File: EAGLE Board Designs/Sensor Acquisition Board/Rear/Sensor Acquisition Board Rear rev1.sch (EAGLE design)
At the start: 26 parts, among them J10 JUMPER_0603_, J4 CONNECTOR-SENSOR_NF_S_RA_BLACK, J5 CONNECTOR-SENSOR_NF_S_RA_BLACK, J6 CONNECTOR-SENSOR_NF_S_RA_BLACK, J7 CONNECTOR-SENSOR_NF_S_RA_BLACK, J9 CONNECTOR-CAN_NF_S_RA_BLACK, U1 VOLTAGE_REGULATOR_SOT-223_5V, U2 MCP2562FD

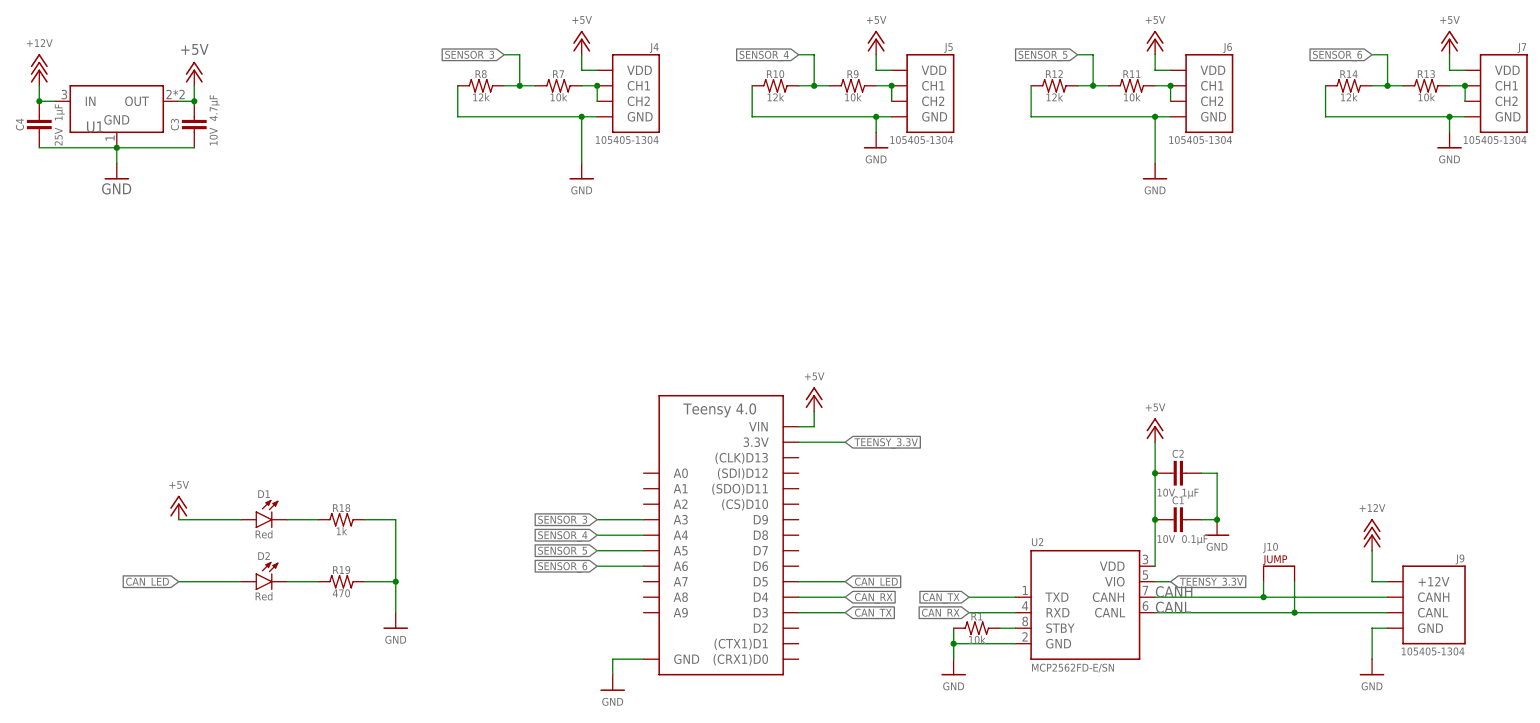
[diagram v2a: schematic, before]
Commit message: corrected Nanofits to Microfits and order files
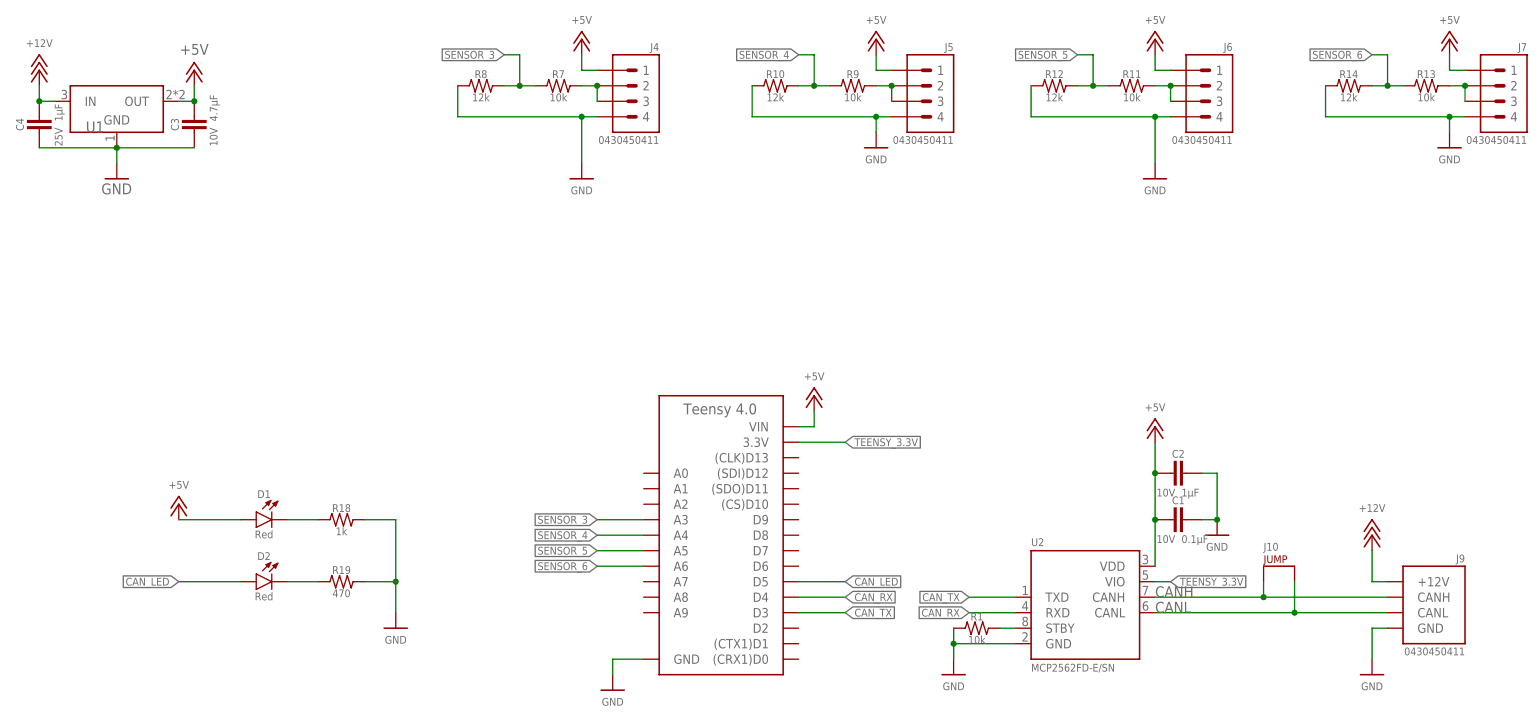
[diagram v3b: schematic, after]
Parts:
- J4, J5, J6, J7: value CONNECTOR-SENSOR_NF_S_RA_BLACK -> CONNECTOR-4_μF_S_RA_; device HyTechDevices:CONNECTOR-SENSOR_NF_S_RA_BLACK -> HyTechDevices:CONNECTOR-4_μF_S_RA_
- J9: value CONNECTOR-CAN_NF_S_RA_BLACK -> CONNECTOR-CAN_μF_S_RA_; device HyTechDevices:CONNECTOR-CAN_NF_S_RA_BLACK -> HyTechDevices:CONNECTOR-CAN_μF_S_RA_
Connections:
- net +5V: now also J4.1, J5.1, J6.1, J7.1; no longer J4.VDD, J5.VDD, J6.VDD, J7.VDD
- net GND: now also J4.4, J5.4, J6.4, J7.4; no longer J4.GND, J5.GND, J6.GND, J7.GND
- net N$5: now also J7.2, J7.3; no longer J7.CH1, J7.CH2
- net N$6: now also J5.2, J5.3; no longer J5.CH1, J5.CH2
- net N$7: now also J6.2, J6.3; no longer J6.CH1, J6.CH2
- net N$9: now also J4.2, J4.3; no longer J4.CH1, J4.CH2
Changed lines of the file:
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@@
 <part name="C2" library="HyTechDevices" deviceset="CAPACITOR_?_*" device="0603" technology="10V_1UF"/>
 <part name="P3" library="HyTechSupplies" deviceset="GND" device=""/>
-<part name="J9" library="HyTechDevices" deviceset="CONNECTOR-CAN_?_*" device="NF_S_RA" technology="BLACK"/>
+<part name="J9" library="HyTechDevices" deviceset="CONNECTOR-CAN_?_*" device="μF_S_RA" value="CONNECTOR-CAN_μF_S_RA_"/>
 <part name="P6" library="HyTechSupplies" deviceset="GND" device=""/>
 <part name="P8" library="HyTechSupplies" deviceset="+12V" device=""/>
@@
 <part name="P9" library="HyTechSupplies" deviceset="GND" device=""/>
 <part name="P10" library="HyTechSupplies" deviceset="+5V" device=""/>
-<part name="J6" library="HyTechDevices" deviceset="CONNECTOR-SENSOR_?_*" device="NF_S_RA" technology="BLACK"/>
-<part name="J5" library="HyTechDevices" deviceset="CONNECTOR-SENSOR_?_*" device="NF_S_RA" technology="BLACK"/>
-<part name="J7" library="HyTechDevices" deviceset="CONNECTOR-SENSOR_?_*" device="NF_S_RA" technology="BLACK"/>
-<part name="J4" library="HyTechDevices" deviceset="CONNECTOR-SENSOR_?_*" device="NF_S_RA" technology="BLACK"/>
+<part name="J6" library="HyTechDevices" deviceset="CONNECTOR-4_?_*" device="μF_S_RA"/>
+<part name="J5" library="HyTechDevices" deviceset="CONNECTOR-4_?_*" device="μF_S_RA"/>
+<part name="J7" library="HyTechDevices" deviceset="CONNECTOR-4_?_*" device="μF_S_RA"/>
+<part name="J4" library="HyTechDevices" deviceset="CONNECTOR-4_?_*" device="μF_S_RA"/>
 <part name="P7" library="HyTechSupplies" deviceset="+5V" device=""/>
 <part name="P11" library="HyTechSupplies" deviceset="+5V" device=""/>
@@
 </segment>
 <segment>
-<pinref part="J5" gate="G$1" pin="GND"/>
+<pinref part="J5" gate="G$1" pin="4"/>
 <wire x1="160.02" y1="190.5" x2="157.48" y2="190.5" width="0.1524" layer="91"/>
 <wire x1="157.48" y1="190.5" x2="157.48" y2="187.96" width="0.1524" layer="91"/>
@@
 </segment>
 <segment>
-<pinref part="J7" gate="G$1" pin="GND"/>
+<pinref part="J7" gate="G$1" pin="4"/>
 <wire x1="254" y1="190.5" x2="251.46" y2="190.5" width="0.1524" layer="91"/>
 <wire x1="251.46" y1="190.5" x2="251.46" y2="187.96" width="0.1524" layer="91"/>
@@
 </segment>
 <segment>
-<pinref part="J6" gate="G$1" pin="GND"/>
+<pinref part="J6" gate="G$1" pin="4"/>
 <wire x1="205.74" y1="190.5" x2="203.2" y2="190.5" width="0.1524" layer="91"/>
 <wire x1="203.2" y1="190.5" x2="203.2" y2="182.88" width="0.1524" layer="91"/>
@@
 </segment>
 <segment>
-<pinref part="J4" gate="G$1" pin="GND"/>
+<pinref part="J4" gate="G$1" pin="4"/>
 <wire x1="111.76" y1="190.5" x2="109.22" y2="190.5" width="0.1524" layer="91"/>
 <wire x1="109.22" y1="190.5" x2="109.22" y2="182.88" width="0.1524" layer="91"/>
@@
 </segment>
 <segment>
-<pinref part="J5" gate="G$1" pin="VDD"/>
+<pinref part="J5" gate="G$1" pin="1"/>
 <wire x1="160.02" y1="198.12" x2="157.48" y2="198.12" width="0.1524" layer="91"/>
 <wire x1="157.48" y1="198.12" x2="157.48" y2="200.66" width="0.1524" layer="91"/>
@@
 </segment>
 <segment>
-<pinref part="J7" gate="G$1" pin="VDD"/>
+<pinref part="J7" gate="G$1" pin="1"/>
 <wire x1="254" y1="198.12" x2="251.46" y2="198.12" width="0.1524" layer="91"/>
 <wire x1="251.46" y1="198.12" x2="251.46" y2="200.66" width="0.1524" layer="91"/>
@@
 </segment>
 <segment>
-<pinref part="J6" gate="G$1" pin="VDD"/>
+<pinref part="J6" gate="G$1" pin="1"/>
 <wire x1="205.74" y1="198.12" x2="203.2" y2="198.12" width="0.1524" layer="91"/>
 <wire x1="203.2" y1="200.66" x2="203.2" y2="198.12" width="0.1524" layer="91"/>
@@
 </segment>
 <segment>
-<pinref part="J4" gate="G$1" pin="VDD"/>
+<pinref part="J4" gate="G$1" pin="1"/>
 <wire x1="111.76" y1="198.12" x2="109.22" y2="198.12" width="0.1524" layer="91"/>
 <wire x1="109.22" y1="198.12" x2="109.22" y2="200.66" width="0.1524" layer="91"/>
@@
 <segment>
 <pinref part="R13" gate="G$1" pin="2"/>
-<pinref part="J7" gate="G$1" pin="CH1"/>
+<pinref part="J7" gate="G$1" pin="2"/>
 <wire x1="251.46" y1="195.58" x2="254" y2="195.58" width="0.1524" layer="91"/>
-<pinref part="J7" gate="G$1" pin="CH2"/>
+<pinref part="J7" gate="G$1" pin="3"/>
 <wire x1="254" y1="195.58" x2="254" y2="193.04" width="0.1524" layer="91"/>
 <junction x="254" y="195.58"/>
@@
 <segment>
 <pinref part="R9" gate="G$1" pin="2"/>
-<pinref part="J5" gate="G$1" pin="CH1"/>
+<pinref part="J5" gate="G$1" pin="2"/>
 <wire x1="157.48" y1="195.58" x2="160.02" y2="195.58" width="0.1524" layer="91"/>
-<pinref part="J5" gate="G$1" pin="CH2"/>
+<pinref part="J5" gate="G$1" pin="3"/>
 <wire x1="160.02" y1="195.58" x2="160.02" y2="193.04" width="0.1524" layer="91"/>
 <junction x="160.02" y="195.58"/>
@@
 <segment>
 <pinref part="R11" gate="G$1" pin="2"/>
-<pinref part="J6" gate="G$1" pin="CH1"/>
+<pinref part="J6" gate="G$1" pin="2"/>
 <wire x1="203.2" y1="195.58" x2="205.74" y2="195.58" width="0.1524" layer="91"/>
-<pinref part="J6" gate="G$1" pin="CH2"/>
+<pinref part="J6" gate="G$1" pin="3"/>
 <wire x1="205.74" y1="195.58" x2="205.74" y2="193.04" width="0.1524" layer="91"/>
 <junction x="205.74" y="195.58"/>
@@
 <segment>
 <pinref part="R7" gate="G$1" pin="2"/>
-<pinref part="J4" gate="G$1" pin="CH1"/>
+<pinref part="J4" gate="G$1" pin="2"/>
 <wire x1="109.22" y1="195.58" x2="111.76" y2="195.58" width="0.1524" layer="91"/>
-<pinref part="J4" gate="G$1" pin="CH2"/>
+<pinref part="J4" gate="G$1" pin="3"/>
 <wire x1="111.76" y1="195.58" x2="111.76" y2="193.04" width="0.1524" layer="91"/>
 <junction x="111.76" y="195.58"/>

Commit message: order files
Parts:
- removed J9: CONNECTOR-CAN_μF_S_RA_, HyTechDevices:CONNECTOR-CAN_μF_S_RA_
- removed R18: RESISTOR_0603_1K, HyTechDevices:RESISTOR_0603_1K
- added J3: CONNECTOR-4_μF_S_RA_, HyTechDevices:CONNECTOR-4_μF_S_RA_
- added R3: RESISTOR_0603_10K, HyTechDevices:RESISTOR_0603_10K
- J6: value CONNECTOR-4_μF_S_RA_ -> CONNECTOR-CAN_μF_S_RA_; device HyTechDevices:CONNECTOR-4_μF_S_RA_ -> HyTechDevices:CONNECTOR-CAN_μF_S_RA_
- R1: value RESISTOR_0603_10K -> RESISTOR_0603_1K; device HyTechDevices:RESISTOR_0603_10K -> HyTechDevices:RESISTOR_0603_1K
- renumbered A2 to A1, J10 to J1, J7 to J2, R12 to R6, R13 to R5, R14 to R4, R19 to R2
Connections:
- net +12V: now also J6.+12V; no longer J9.+12V
- net +5V: now also J3.1; no longer J6.1
- net CANH: now also J6.CANH; no longer J9.CANH
- net CANL: now also J6.CANL; no longer J9.CANL
- net GND: now also J3.4, J6.GND, R1.2, R3.1; no longer J6.4, J9.GND, R1.1, R18.2
- net N$1: now also R1.1; no longer R18.1
- net N$3: now also R3.2; no longer R1.2
- net N$6: now also J4.2, J4.3; no longer J5.2, J5.3
- net N$7: now also J3.2, J3.3, R7.2; no longer J6.2, J6.3, R11.2
- net N$9: now also J5.2, J5.3, R11.2; no longer J4.2, J4.3, R7.2
- net SENSOR_3: now also R10.2, R11.1; no longer R7.1, R8.2
- net SENSOR_4: now also R8.2; no longer R10.2
- net SENSOR_5: now also R7.1; no longer R11.1
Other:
- moved on the sheet: J4, J5, R1, R10, R11, R7, R8

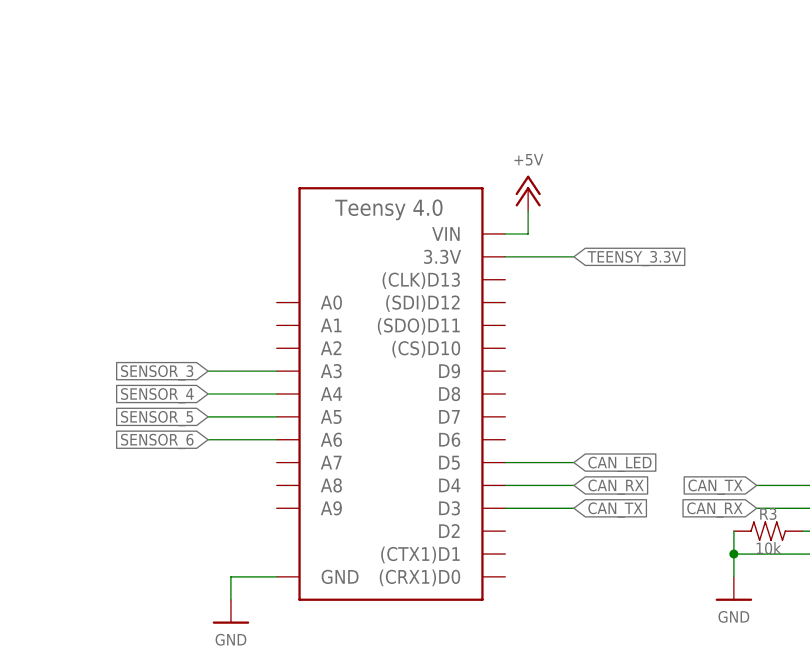
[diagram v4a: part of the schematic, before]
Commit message: Replaced SAB Rear 4.0 with 3.2
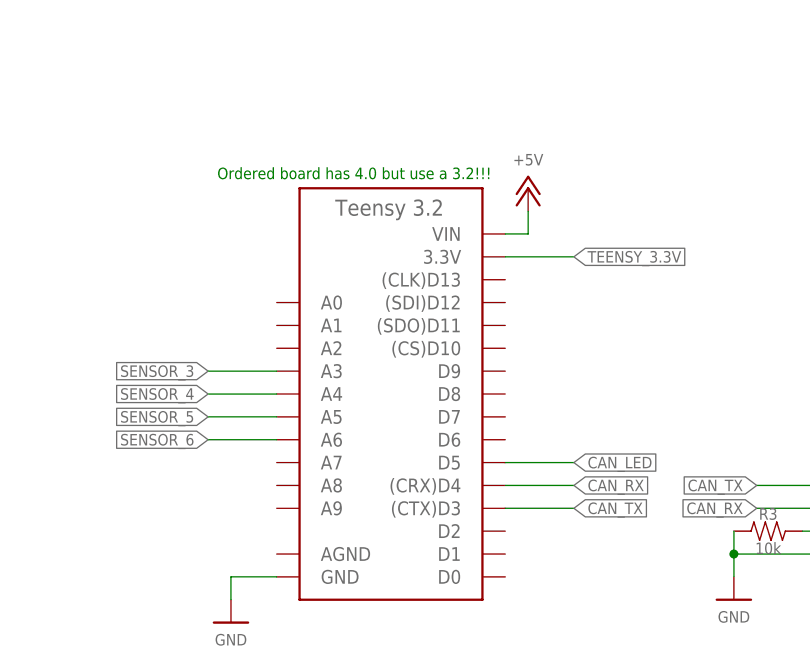
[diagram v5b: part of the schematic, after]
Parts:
- A1: value TEENSY_4.0 -> TEENSY_3.2; device HyTechDevices:TEENSY_4.0 -> HyTechDevices:TEENSY_3.2
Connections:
- net CAN_RX: now also A1.(CRX)D4; no longer A1.D4
- net CAN_TX: now also A1.(CTX)D3; no longer A1.D3
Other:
- note added: "Ordered board has 4.0 but use a 3.2!!!"
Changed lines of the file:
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@@
 <part name="R5" library="HyTechDevices" deviceset="RESISTOR_?_*" device="0603" technology="10K" value="RESISTOR_0603_10K"/>
 <part name="R4" library="HyTechDevices" deviceset="RESISTOR_?_*" device="0603" technology="12K" value="RESISTOR_0603_12K"/>
-<part name="A1" library="HyTechDevices" deviceset="TEENSY_4.0" device=""/>
+<part name="A1" library="HyTechDevices" deviceset="TEENSY_3.2" device=""/>
 <part name="U2" library="HyTechDevices" deviceset="MCP2562FD" device=""/>
 <part name="R3" library="HyTechDevices" deviceset="RESISTOR_?_*" device="0603" technology="10K"/>
@@
 <sheet>
 <plain>
+<text x="112.776" y="145.796" size="1.27" layer="91" font="vector">Ordered board has 4.0 but use a 3.2!!!</text>
 </plain>
 <instances>
@@
 <wire x1="144.78" y1="111.76" x2="152.4" y2="111.76" width="0.1524" layer="91"/>
 <label x="152.4" y="111.76" size="1.27" layer="95" xref="yes"/>
-<pinref part="A1" gate="G$1" pin="D4"/>
+<pinref part="A1" gate="G$1" pin="(CRX)D4"/>
 </segment>
 <segment>
@@
 <wire x1="144.78" y1="109.22" x2="152.4" y2="109.22" width="0.1524" layer="91"/>
 <label x="152.4" y="109.22" size="1.27" layer="95" xref="yes"/>
-<pinref part="A1" gate="G$1" pin="D3"/>
-</segment>
-<segment>
+<pinref part="A1" gate="G$1" pin="(CTX)D3"/>
+</segment>
+<segment>
